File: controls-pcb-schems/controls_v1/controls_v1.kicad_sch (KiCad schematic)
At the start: 13 parts, among them J1 Raspberry_Pi_4, U2 MS5607-02BA, U3 DRV5053EAQLPG

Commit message: more schematic wiring updates
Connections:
- net to_Sensors is gone; now on net Sensors_Vin: DFR1. (VOUT+)
- net +3.3V: now also IC1.10 (VS)
- net GND: now also IC1.11 (GND), IC1.13 (GND), IC1.6 (GND)
- net at BIGTREEETECH_TMC5160T1.4 (DIAG0): now also J1.12 (GPIO18/SPI1_~{CE0}/PCM_CLK/PWM0)
- net at BIGTREEETECH_TMC5160T1.5 (DIAG1): now also J1.35 (GPIO19/SPI1_MISO/PCM_FS), MIKROE-1.P5 (MISO), MIKROE-2.P5 (MISO)
- net Sensors_Vin: now reaches DFR1. (VOUT+)
- net at J1.27 (ID_SD_I2C0/GPIO00): now also IC1.8 (SDA)
- net at J1.28 (ID_SC_I2C0/GPIO01): now also IC1.9 (SCL)
- net Motor_Battery+: now reaches IC1.1 (IN+), IC1.2 (IN+), IC1.3 (IN+)
- net Motor_Power_In: now reaches IC1.14 (IN-), IC1.15 (IN-), IC1.16 (IN-)
- no-connect marks 15 -> 17
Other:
- moved on the sheet: DFR1, DFR2, IC2, IC3, U2, U3

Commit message: I added a symbol for the Adafruit GPS PA101
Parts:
- added U5: (no value), Footprints:Adafruit GPS PA101, symbol Symbols:Adafruit GPS PA1010D
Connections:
- net at BIGTREEETECH_TMC5160T1.4 (DIAG0): now also J1.12 (GPIO18/SPI1_~{CE0}/PCM_CLK/PWM0)
- net at BIGTREEETECH_TMC5160T1.5 (DIAG1): now also J1.35 (GPIO19/SPI1_MISO/PCM_FS), MIKROE-1.P5 (MISO), MIKROE-2.P5 (MISO)
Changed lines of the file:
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@@
+	)
+	(symbol
+		(lib_id "Symbols:Adafruit GPS PA1010D")
+		(at 109.22 52.07 0)
+		(unit 1)
+		(body_style 1)
+		(exclude_from_sim no)
+		(in_bom yes)
+		(on_board yes)
+		(in_pos_files yes)
+		(dnp no)
+		(fields_autoplaced yes)
+		(property "Reference" "U5"
+			(at 109.22 53.34 0)
+			(show_name no)
+			(do_not_autoplace no)
+			(effects
+				(font
+					(size 1.27 1.27)
+				)
+			)
+		)
+		(property "Value" ""
+			(at 109.22 52.07 0)
+			(show_name no)
+			(do_not_autoplace no)
+			(effects
+				(font
+					(size 1.27 1.27)
+				)
+			)
+		)
+		(property "Footprint" "Footprints:Adafruit GPS PA101"
+			(at 109.22 52.07 0)
+			(hide yes)
+			(show_name no)
+			(do_not_autoplace no)
+			(effects
+				(font
+					(size 1.27 1.27)
+				)
+			)
+		)
+		(property "Datasheet" ""
+			(at 109.22 52.07 0)
+			(hide yes)
+			(show_name no)
+			(do_not_autoplace no)
+			(effects
+				(font
+					(size 1.27 1.27)
+				)
+			)
+		)
+		(property "Description" ""
+			(at 109.22 52.07 0)
+			(hide yes)
+			(show_name no)
+			(do_not_autoplace no)
+			(effects
+				(font
+					(size 1.27 1.27)
+				)
+			)
+		)
+		(pin "9"
+		)
+		(pin "8"
+		)
+		(pin "4"
+		)
+		(pin "3"
+		)
+		(pin "10"
+		)
+		(pin "1"
+		)
+		(pin "5"
+		)
+		(pin "2"
+		)
+		(pin "6"
+		)
+		(pin "7"
+		)
+		(instances
+			(project "controls_v1"
+				(path "/5dd72d53-dc48-4296-8d46-03ae548cca02"
+					(reference "U5")
+					(unit 1)
+				)
+			)
+		)
 	)
 	(symbol

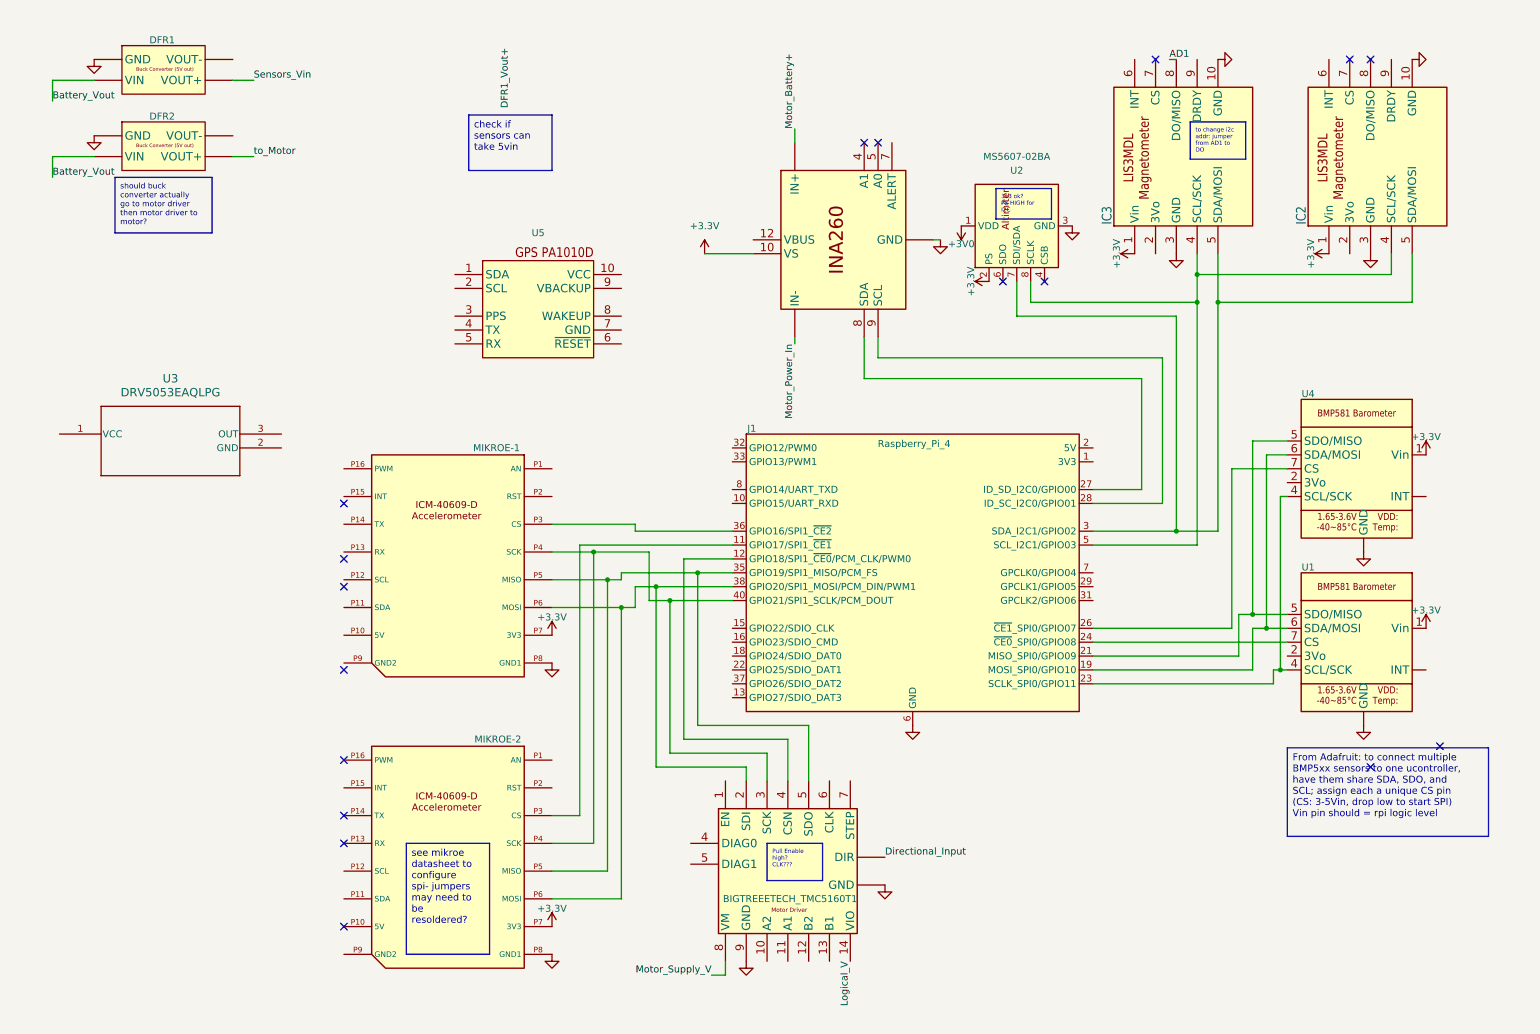
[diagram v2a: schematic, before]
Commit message: cleaned up lines, added RRC3+, added reverse polarity protection, added labelling in some places
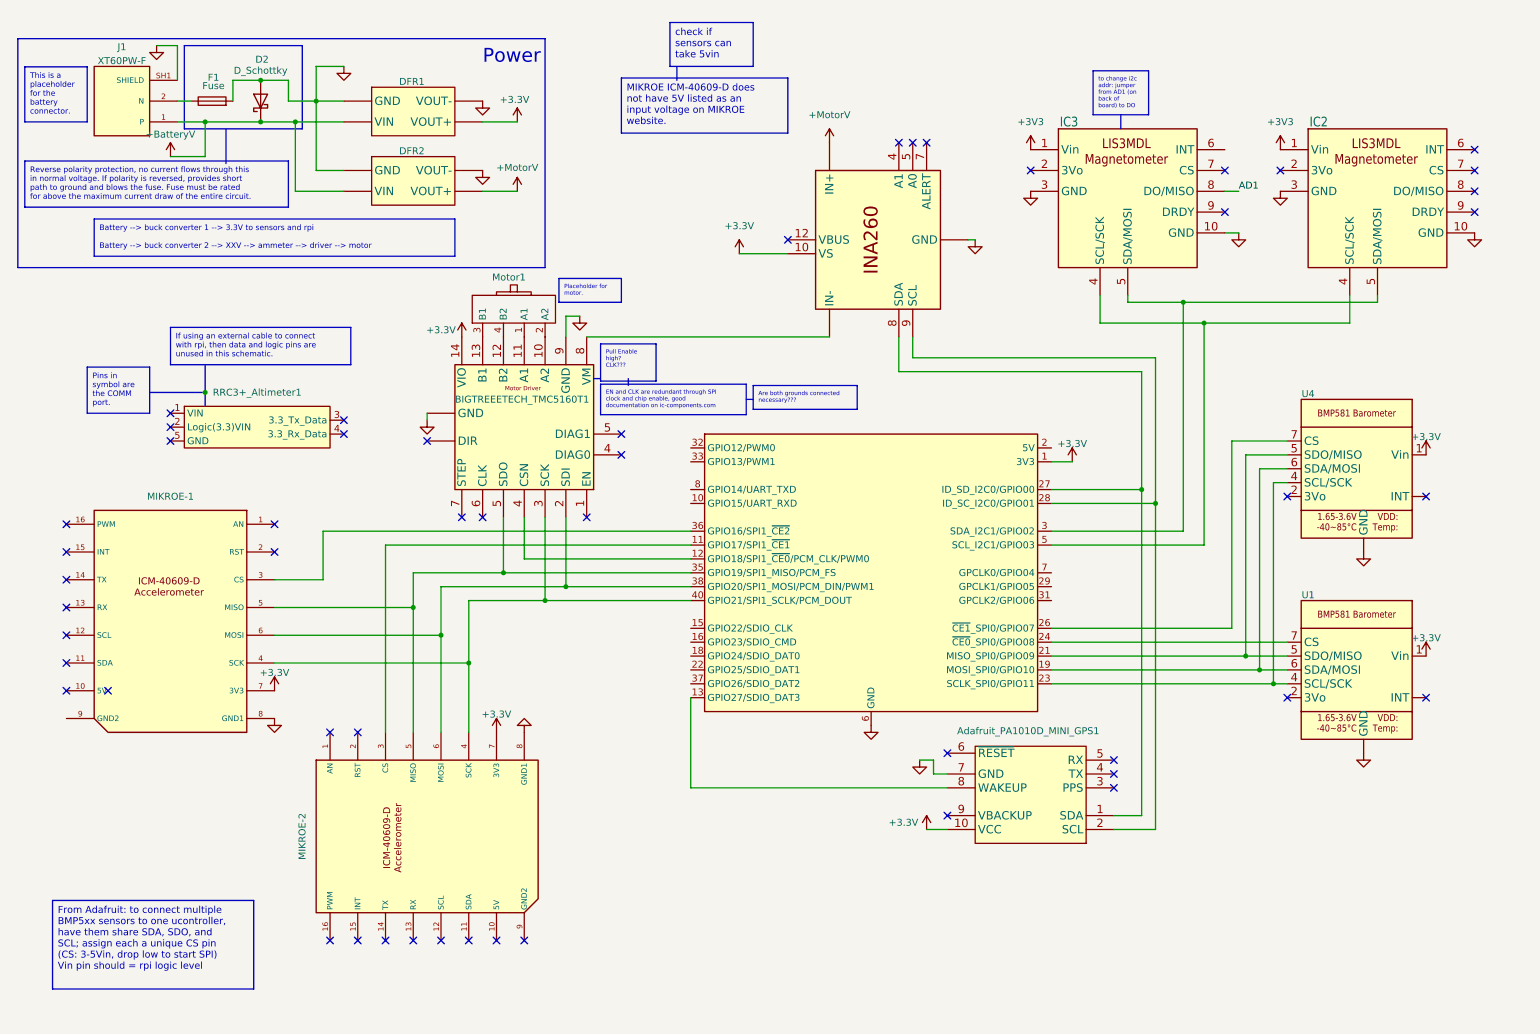
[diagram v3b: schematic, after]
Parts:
- removed J1: Raspberry_Pi_4, Package_DFN_QFN:QFN-56-1EP_7x7mm_P0.4mm_EP3.2x3.2mm, symbol Connector:Raspberry_Pi_4
- removed MIKROE-1, MIKROE-2: (no value), Controls_EECS_Footprints:MIKROBUS_MODULE_CONN, symbol Controls_EECS:MIKROE-6420
- removed U2: MS5607-02BA, Package_LGA:LGA-8_3x5mm_P1.25mm, symbol Sensor_Pressure:MS5607-02BA
- removed U3: DRV5053EAQLPG, Package_TO_SOT_THT:TO-92S, symbol Controls_EECS:DRV5053EAQLPG
- removed U5: (no value), Footprints:Adafruit GPS PA101, symbol Symbols:Adafruit GPS PA1010D
- added Adafruit_PA1010D_MINI_GPS1: (no value), Controls_EECS:Adafruit_PA1010D_Mini_GPS, symbol symbols:Adafruit_PA1010D_Mini_Gps
- added D2: D_Schottky, Diode_SMD:D_3220_8050Metric_Pad2.65x5.15mm_HandSolder, symbol Device:D_Schottky
- added F1: Fuse, Fuse:Fuseholder_Cylinder-5x20mm_Stelvio-Kontek_PTF78_Horizontal_Open, symbol Device:Fuse
- added J1: XT60PW-F, Connector_AMASS:AMASS_XT60PW-M_1x02_P7.20mm_Horizontal, symbol Symbols:XT60PW-F
- added MIKROE-1, MIKROE-2: (no value), ControlsEECS:MIKROBUS_MODULE_CONN, symbol Symbols:MIKROE-6420
- added Motor1: (no value), symbol Symbols:Motor_Placeholder
- added RRC3+_Altimeter1: (no value), Controls_EECS:RRC3+ Altimeter, symbol Symbols:RRC3+_Altimeter
- added U6: (no value), Controls_EECS:Raspberry Pi 4 Pins, symbol symbols:Raspberry_Pi_4
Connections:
- net Battery_Vout is gone; now on net GND: DFR1. (VOUT+), DFR2. (VOUT+)
- net Directional_Input is gone; now on net GND: BIGTREEETECH_TMC5160T1.2 (GND)
- net Logical_V is gone; now on net +3.3V: BIGTREEETECH_TMC5160T1.14 (VIO)
- net Motor_Supply_V is gone; now on an unnamed net: BIGTREEETECH_TMC5160T1.8 (VM)
- net Sensors_Vin is gone; now on net GND: DFR1. (VOUT+)
- net to_Motor is gone; now on net GND: DFR2. (VOUT+)
- net +3.3V: now also DFR1. (VOUT+), Adafruit_PA1010D_MINI_GPS1.10 (VCC), MIKROE-1.7 (3V3), MIKROE-2.7 (3V3), U6.1 (3V3), U6.17 (3V3); no longer IC2.1 (Vin), IC3.1 (Vin)
- net GND: now also Adafruit_PA1010D_MINI_GPS1.7 (GND), D2.2 (A), F1.2, J1.SH1 (SHIELD), J1.SH2 (SHIELD), MIKROE-1.8 (GND1), MIKROE-2.8 (GND1), U6.14 (GND), U6.20 (GND), U6.25 (GND), U6.30 (GND), U6.34 (GND), U6.39 (GND), U6.6 (GND), U6.9 (GND)
- net at IC2.4 (SCL/SCK), IC3.4 (SCL/SCK): now also U6.5 (SCL_I2C1/GPIO03)
- net at IC2.5 (SDA/MOSI), IC3.5 (SDA/MOSI): now also U6.3 (SDA_I2C1/GPIO02)
- net at BIGTREEETECH_TMC5160T1.10 (A2): now also Motor1.2 (A2)
- net at BIGTREEETECH_TMC5160T1.11 (A1): now also Motor1.1 (A1)
- net at BIGTREEETECH_TMC5160T1.12 (B2): now also Motor1.4 (B2)
- net at BIGTREEETECH_TMC5160T1.13 (B1): now also Motor1.3 (B1)
- net at BIGTREEETECH_TMC5160T1.3 (SCK): now also MIKROE-1.4 (SCK), MIKROE-2.4 (SCK), U6.40 (GPIO21/SPI1_SCLK/PCM_DOUT)
- net at BIGTREEETECH_TMC5160T1.4 (DIAG0): now also U6.12 (GPIO18/SPI1_~{CE0}/PCM_CLK/PWM0)
- net at U1.4 (SCL/SCK), U4.4 (SCL/SCK): now also U6.23 (SCLK_SPI0/GPIO11)
- net at U1.5 (SDO/MISO), U4.5 (SDO/MISO): now also U6.21 (MISO_SPI0/GPIO09)
- net at U1.6 (SDA/MOSI), U4.6 (SDA/MOSI): now also U6.19 (MOSI_SPI0/GPIO10)
- net at U1.7 (CS): now also U6.24 (~{CE0}_SPI0/GPIO08)
- net at U4.7 (CS): now also U6.26 (~{CE1}_SPI0/GPIO07)
- net at IC1.8 (SDA): now also Adafruit_PA1010D_MINI_GPS1.1 (SDA), U6.27 (ID_SD_I2C0/GPIO00)
- net at IC1.9 (SCL): now also Adafruit_PA1010D_MINI_GPS1.2 (SCL), U6.28 (ID_SC_I2C0/GPIO01)
- net Motor_Battery+ renamed +MotorV
- net +MotorV: now also DFR2. (VOUT+)
- net Motor_Power_In: no longer names the net of IC1.14 (IN-), IC1.15 (IN-), IC1.16 (IN-)
- new net: MIKROE-2.3 (CS), U6.11 (GPIO17/SPI1_~{CE1})
- new net: BIGTREEETECH_TMC5160T1.5 (DIAG1), MIKROE-1.5 (MISO), MIKROE-2.5 (MISO), U6.35 (GPIO19/SPI1_MISO/PCM_FS)
- new net: BIGTREEETECH_TMC5160T1.2 (GND), MIKROE-1.6 (MOSI), MIKROE-2.6 (MOSI), U6.38 (GPIO20/SPI1_MOSI/PCM_DIN/PWM1)
- new net: F1.1, J1.2 (N)
- new net: MIKROE-1.3 (CS), U6.36 (GPIO16/SPI1_~{CE2})
- new net: Adafruit_PA1010D_MINI_GPS1.8 (WAKEUP), U6.13 (GPIO27/SDIO_DAT3)
- new net: U6.2 (5V), U6.4 (5V)
- new net +3V3: IC2.1 (Vin), IC3.1 (Vin)
- new net +BatteryV: D2.1 (K), DFR1. (VOUT+), DFR2. (VOUT+), J1.1 (P)
- now unconnected: BIGTREEETECH_TMC5160T1.5 (DIAG1)
- no-connect marks 17 -> 52
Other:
- note added: "Power"
- moved on the sheet: BIGTREEETECH_TMC5160T1, IC2, IC3, U1

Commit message: latest schematic changes
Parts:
- added U2: (no value), ControlsEECS:Adafruit LIS3MDL, symbol Controls_EECS:Rotation_Placeholder
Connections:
- net +3.3V: now also RRC3+_Altimeter1.2 (Logic(3.3)VIN), U2.3 (Power)
- net GND: now also BIGTREEETECH_TMC5160T1.6 (CLK), RRC3+_Altimeter1.5 (GND), U2.4 (GND)
- net at IC2.4 (SCL/SCK), IC3.4 (SCL/SCK), U6.5 (SCL_I2C1/GPIO03): now also U2.2 (SCL)
- net at IC2.5 (SDA/MOSI), IC3.5 (SDA/MOSI), U6.3 (SDA_I2C1/GPIO02): now also U2.1 (SDA)
- net at MIKROE-2.2 (RST): now also U6.37 (GPIO26/SDIO_DAT2)
- net at MIKROE-1.2 (RST): now also U6.22 (GPIO25/SDIO_DAT1)
- net at BIGTREEETECH_TMC5160T1.4 (DIAG0): now also U6.12 (GPIO18/SPI1_~{CE0}/PCM_CLK/PWM0)
- net at U6.10 (GPIO15/UART_RXD): now also RRC3+_Altimeter1.3 (3.3_Tx_Data)
- net at U6.8 (GPIO14/UART_TXD): now also RRC3+_Altimeter1.4 (3.3_Rx_Data)
- no-connect marks 52 -> 45
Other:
- moved on the sheet: BIGTREEETECH_TMC5160T1, Motor1

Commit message: all pinouts checked
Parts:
- added DFR3: (no value), Controls_EECS_Footprints:DFR0831 DC-DC, symbol Controls_EECS:DFR0831 DC-DC
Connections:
- net +BatteryV: now also DFR3. (VOUT+)
- net GND: now also DFR3. (VOUT+)
- net at BIGTREEETECH_TMC5160T1.4 (DIAG0): now also U6.12 (GPIO18/SPI1_~{CE0}/PCM_CLK/PWM0)
- net +5V: now reaches U6.2 (5V), U6.4 (5V)
- net +5V: now also DFR3. (VOUT+)
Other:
- moved on the sheet: DFR2

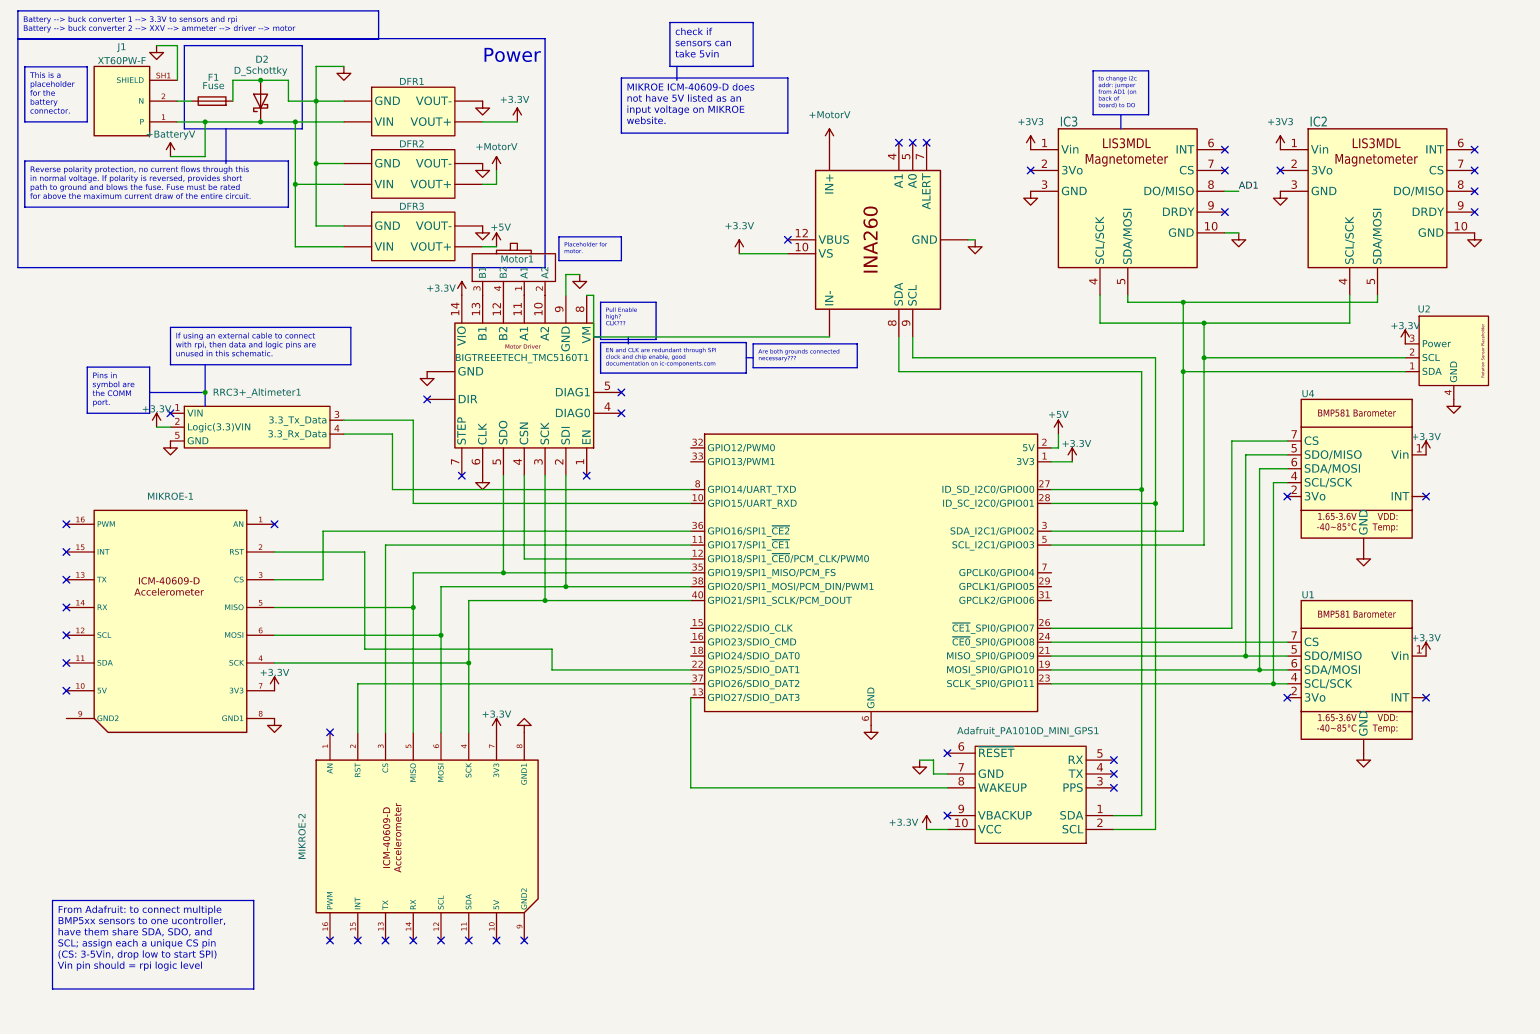
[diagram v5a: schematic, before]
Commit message: switched duplicate sensors to different comm busses
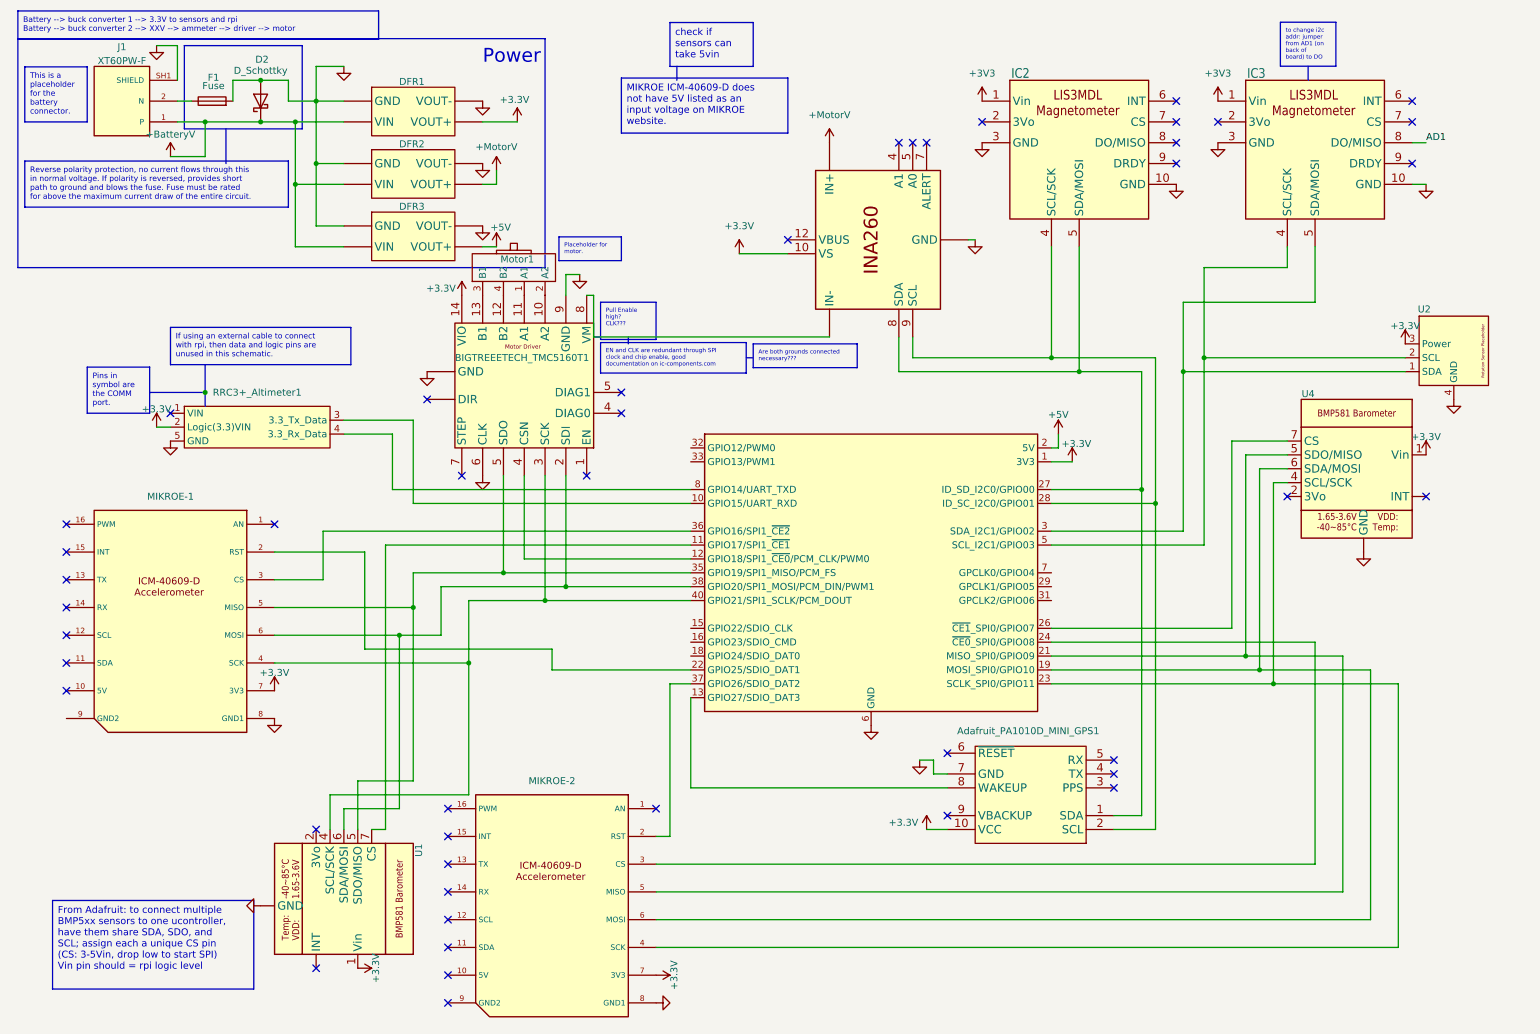
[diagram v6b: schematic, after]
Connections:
- net at IC3.4 (SCL/SCK), U2.2 (SCL), U6.5 (SCL_I2C1/GPIO03): no longer IC2.4 (SCL/SCK)
- net at IC3.5 (SDA/MOSI), U2.1 (SDA), U6.3 (SDA_I2C1/GPIO02): no longer IC2.5 (SDA/MOSI)
- net at MIKROE-2.3 (CS): now also U6.24 (~{CE0}_SPI0/GPIO08); no longer U6.11 (GPIO17/SPI1_~{CE1})
- net at BIGTREEETECH_TMC5160T1.3 (SCK), MIKROE-1.4 (SCK), U6.40 (GPIO21/SPI1_SCLK/PCM_DOUT): now also U1.4 (SCL/SCK); no longer MIKROE-2.4 (SCK)
- net at BIGTREEETECH_TMC5160T1.5 (DIAG1), MIKROE-1.5 (MISO), U6.35 (GPIO19/SPI1_MISO/PCM_FS): now also U1.5 (SDO/MISO); no longer MIKROE-2.5 (MISO)
- net at BIGTREEETECH_TMC5160T1.2 (GND), MIKROE-1.6 (MOSI), U6.38 (GPIO20/SPI1_MOSI/PCM_DIN/PWM1): now also U1.6 (SDA/MOSI); no longer MIKROE-2.6 (MOSI)
- net at Adafruit_PA1010D_MINI_GPS1.1 (SDA), IC1.8 (SDA), U6.27 (ID_SD_I2C0/GPIO00): now also IC2.5 (SDA/MOSI)
- net at Adafruit_PA1010D_MINI_GPS1.2 (SCL), IC1.9 (SCL), U6.28 (ID_SC_I2C0/GPIO01): now also IC2.4 (SCL/SCK)
- net at BIGTREEETECH_TMC5160T1.4 (DIAG0): now also U6.12 (GPIO18/SPI1_~{CE0}/PCM_CLK/PWM0)
- net at U4.4 (SCL/SCK), U6.23 (SCLK_SPI0/GPIO11): now also MIKROE-2.4 (SCK); no longer U1.4 (SCL/SCK)
- net at U4.5 (SDO/MISO), U6.21 (MISO_SPI0/GPIO09): now also MIKROE-2.5 (MISO); no longer U1.5 (SDO/MISO)
- net at U4.6 (SDA/MOSI), U6.19 (MOSI_SPI0/GPIO10): now also MIKROE-2.6 (MOSI); no longer U1.6 (SDA/MOSI)
- net at U1.7 (CS): now also U6.11 (GPIO17/SPI1_~{CE1}); no longer U6.24 (~{CE0}_SPI0/GPIO08)
